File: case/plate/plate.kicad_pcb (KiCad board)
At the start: 2 copper layers, 114.3 x 95.2 mm, 36 parts

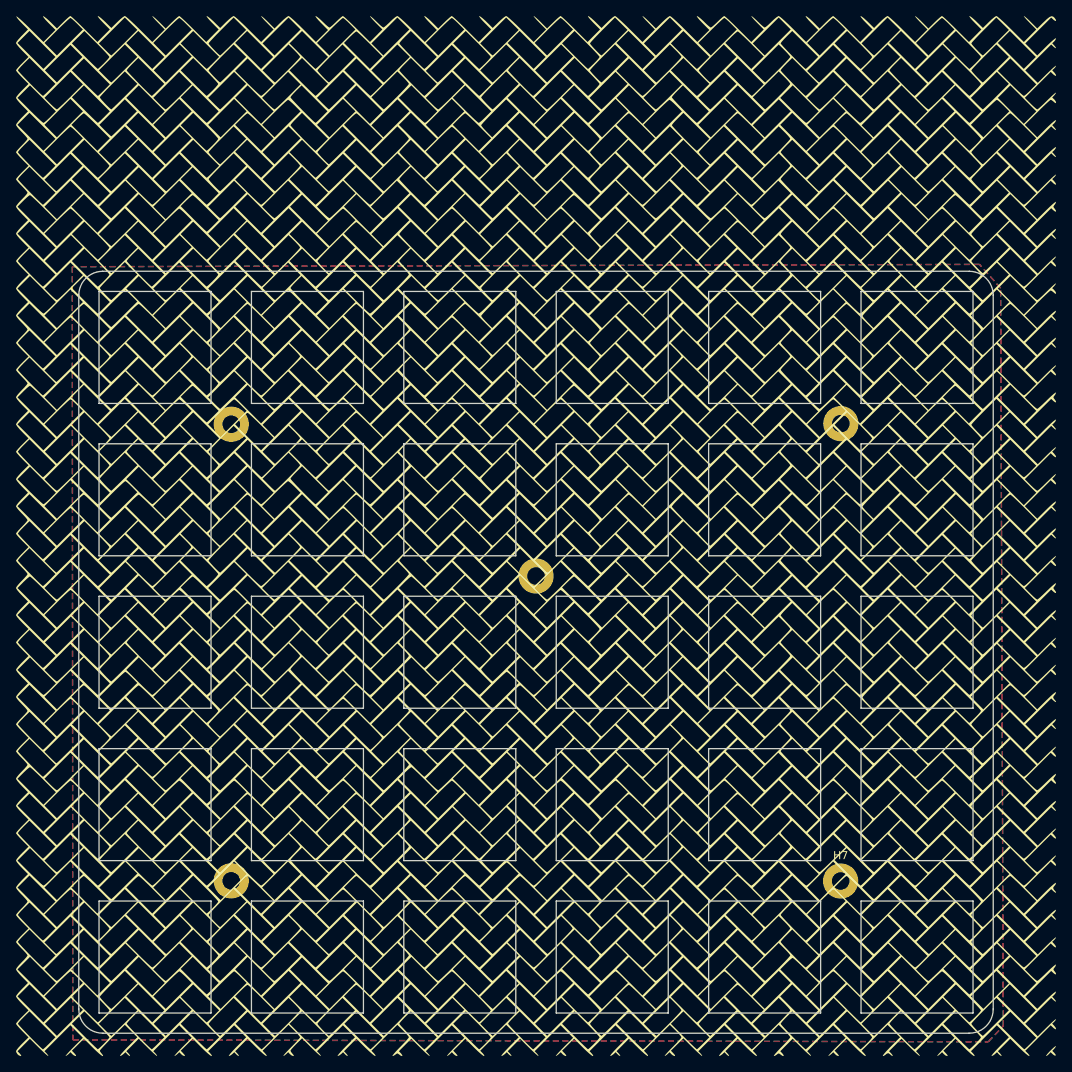
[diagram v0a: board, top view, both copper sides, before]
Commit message: Move kicad projects to subfolders.
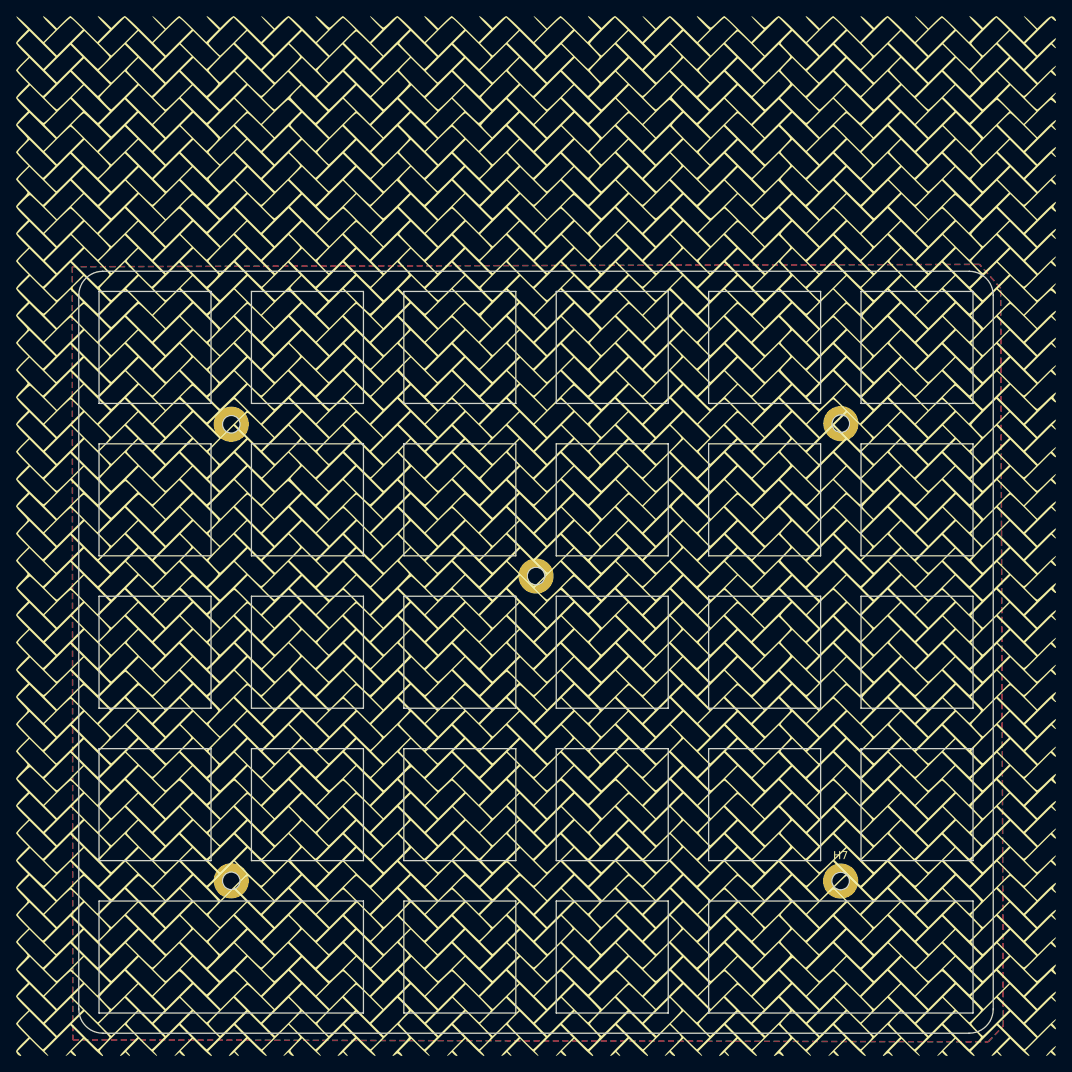
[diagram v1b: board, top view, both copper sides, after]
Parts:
- removed S0_4, S1_4, S4_4, S5_4: Keyswitch, ScottoKeebs_Cutout:Cutout_MX_1.00u
- S0_0, S0_1, S0_2, S0_3, S1_0, S1_1, S1_2, S1_3, S2_0, S2_1, S2_2, S2_3, S2_4, S3_0, S3_1, S3_2, S3_3, S3_4, S4_0, S4_1, S4_2, S4_3, S5_0, S5_1, S5_2, S5_3: footprint ScottoKeebs_Cutout:Cutout_MX_1.00u -> herringbone:Cutout_MX_1.00u
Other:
- outline, holes or cut-outs redrawn

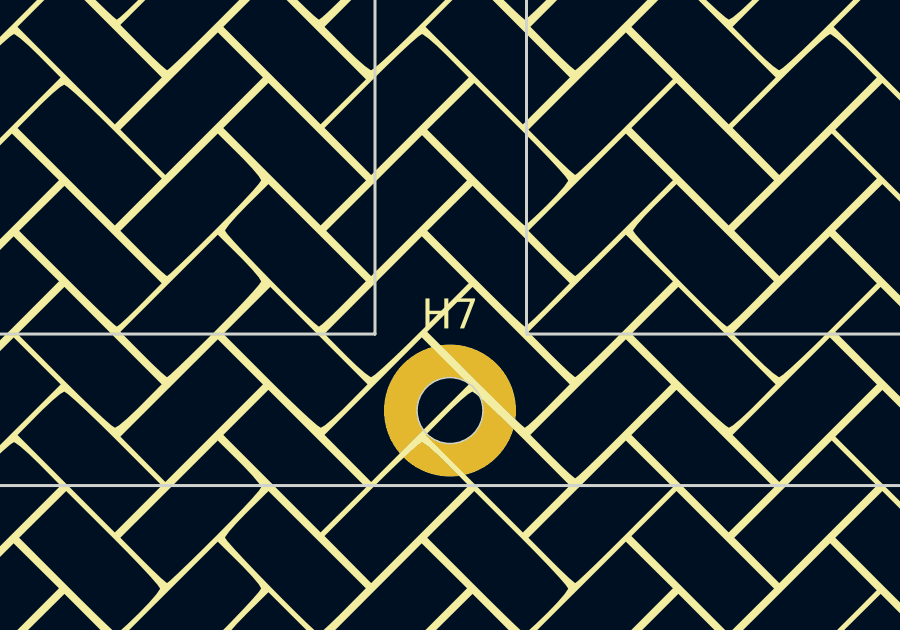
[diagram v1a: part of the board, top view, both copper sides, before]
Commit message: PCB rev2.
- Add LEDs
- Fix D+ D- USB pins for USBaspLoader to be happy
- Widen power Lines
- Allow for 2U keys in bottom corners
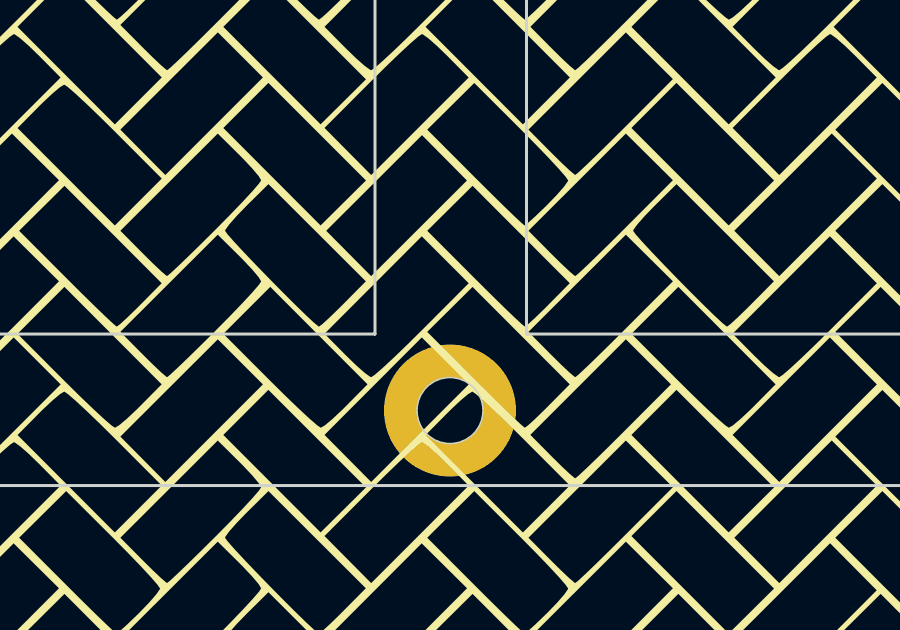
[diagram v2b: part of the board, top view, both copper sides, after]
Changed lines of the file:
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@@
 			(at 0 3.2 0)
 			(layer "F.Fab")
+			(hide yes)
 			(effects
 				(font
@@
 			(at 0 -3.2 0)
 			(layer "F.SilkS")
+			(hide yes)
 			(effects
 				(font
@@
 			(at 0 3.2 0)
 			(layer "F.Fab")
+			(hide yes)
 			(effects
 				(font
